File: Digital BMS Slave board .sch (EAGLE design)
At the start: 259 parts, among them J1 S4B-PH-K, J10 S3B-PH-K, J11 S6B-PH-K, J12 MOLEX22-12-406205-7068, J2 S4B-PH-K, J3 S4B-PH-K, J4 S4B-PH-K, J5 S2B-PH-K, J6 S2B-PH-K, J7 S2B-PH-K, J8 S2B-PH-K, J9 S3B-PH-K, Q1 BSS123, Q2 BSS123, Q3 BSS123, Q4 BSS123, Q5 BSS123, Q6 BSS123, SW1 6PIN-DIP-SWITCH, U1 BQ79606A-Q1-HTQFP|48|9VIA, X1 PESD2CAN, X2 PESD2CAN, X3 PESD2CAN, X4 PESD2CAN

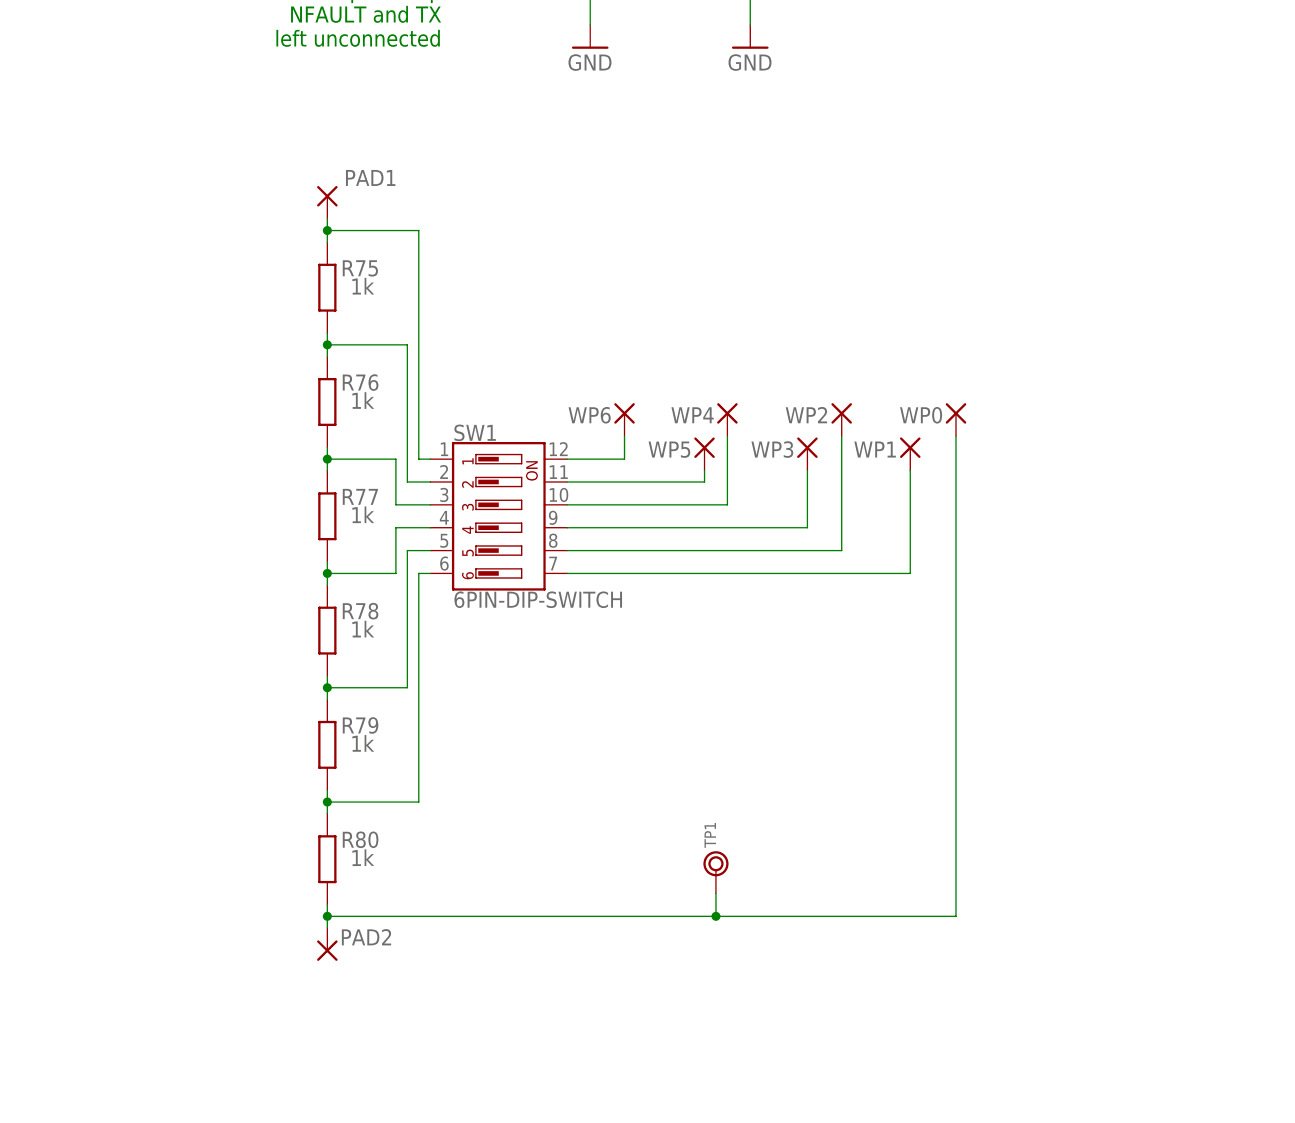
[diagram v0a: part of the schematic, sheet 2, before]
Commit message: Connectors to resistor ladder added
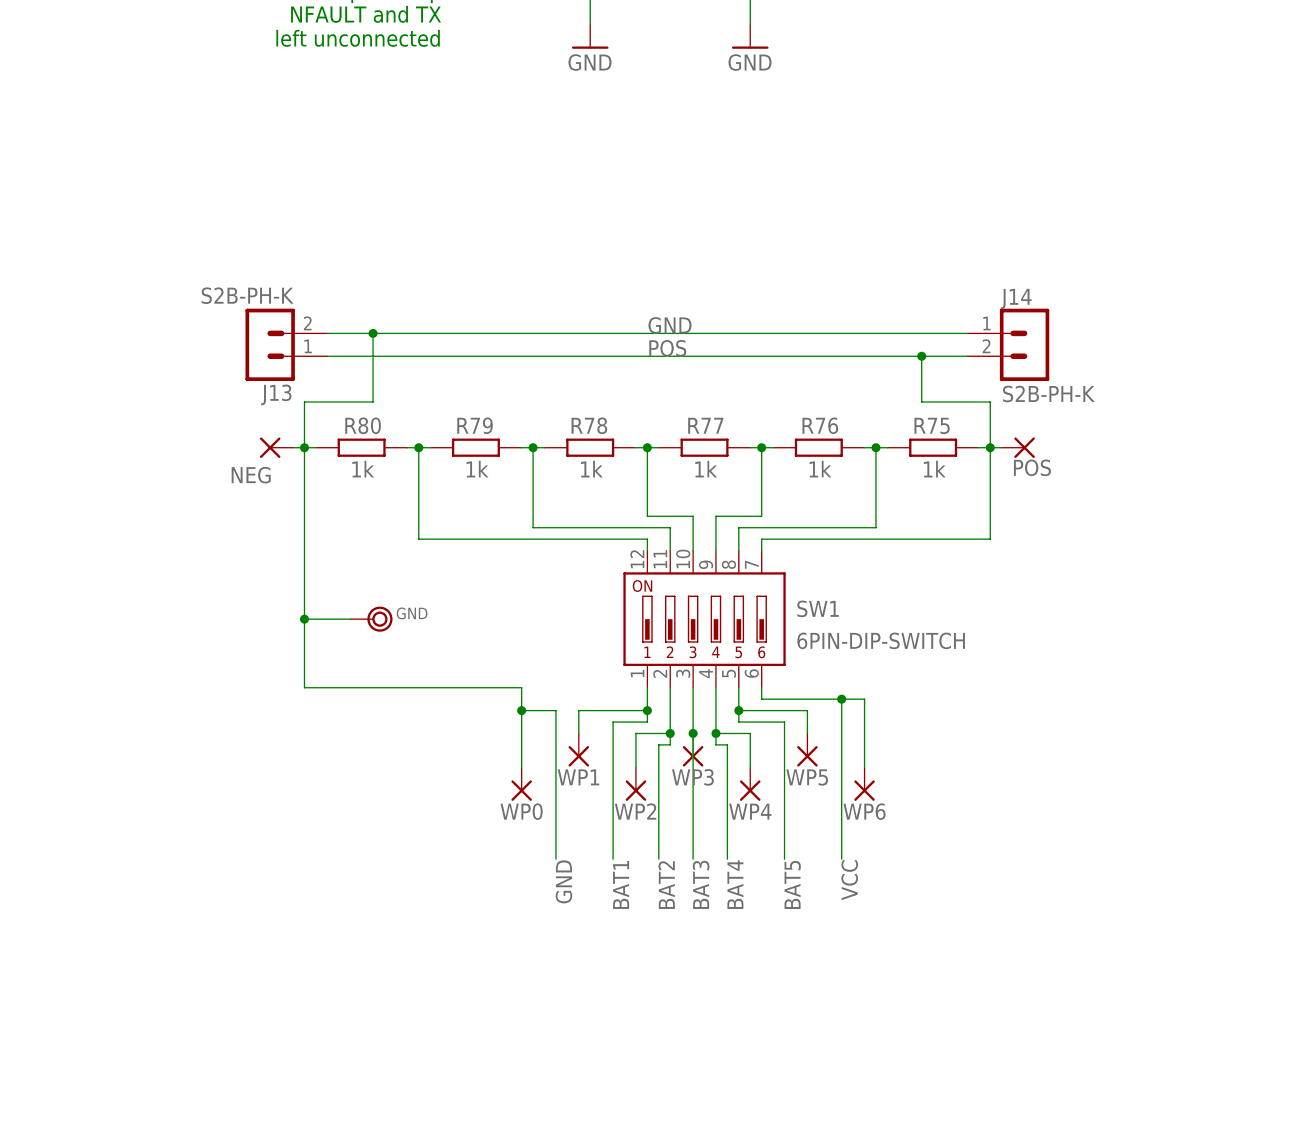
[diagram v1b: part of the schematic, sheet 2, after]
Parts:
- removed PAD1, PAD2: (no value), testing:SMD_PAD
- removed TP1: TEST_RING, testing:TEST_RING
- added GND: TEST_RING, testing:TEST_RING
- added J13, J14: S2B-PH-K, con-jst-ph:S2B-PH-K
- added NEG, POS: (no value), testing:SMD_PAD
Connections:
- removed net N$10: PAD1.P, R75.1, SW1.1
- removed net N$11: PAD2.P, R80.2, TP1.P$1, WP0.P
- removed net N$15: SW1.9, WP3.P
- removed net N$16: SW1.8, WP2.P
- removed net N$17: SW1.7, WP1.P
- removed net N$4: SW1.12, WP6.P
- removed net N$5: SW1.11, WP5.P
- removed net N$7: SW1.10, WP4.P
- new net POS: J13.1, J14.2, POS.P, R75.1, SW1.7
- net BAT1: now also SW1.1, WP1.P
- net BAT2: now also SW1.2, WP2.P
- net BAT3: now also SW1.3, WP3.P
- net BAT4: now also SW1.4, WP4.P
- net BAT5: now also SW1.5, WP5.P
- net GND: now also GND.P$1, J13.2, J14.1, NEG.P, R80.2, WP0.P
- net N$13: now also SW1.12; no longer SW1.6
- net N$14: now also SW1.11; no longer SW1.5
- net N$6: now also SW1.10; no longer SW1.4
- net N$8: now also SW1.9; no longer SW1.3
- net N$9: now also SW1.8; no longer SW1.2
- net VCC: now also SW1.6, WP6.P
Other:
- moved on the sheet: R75, R76, R77, R78, R79, R80, SW1, WP0, WP1, WP2, WP3, WP4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

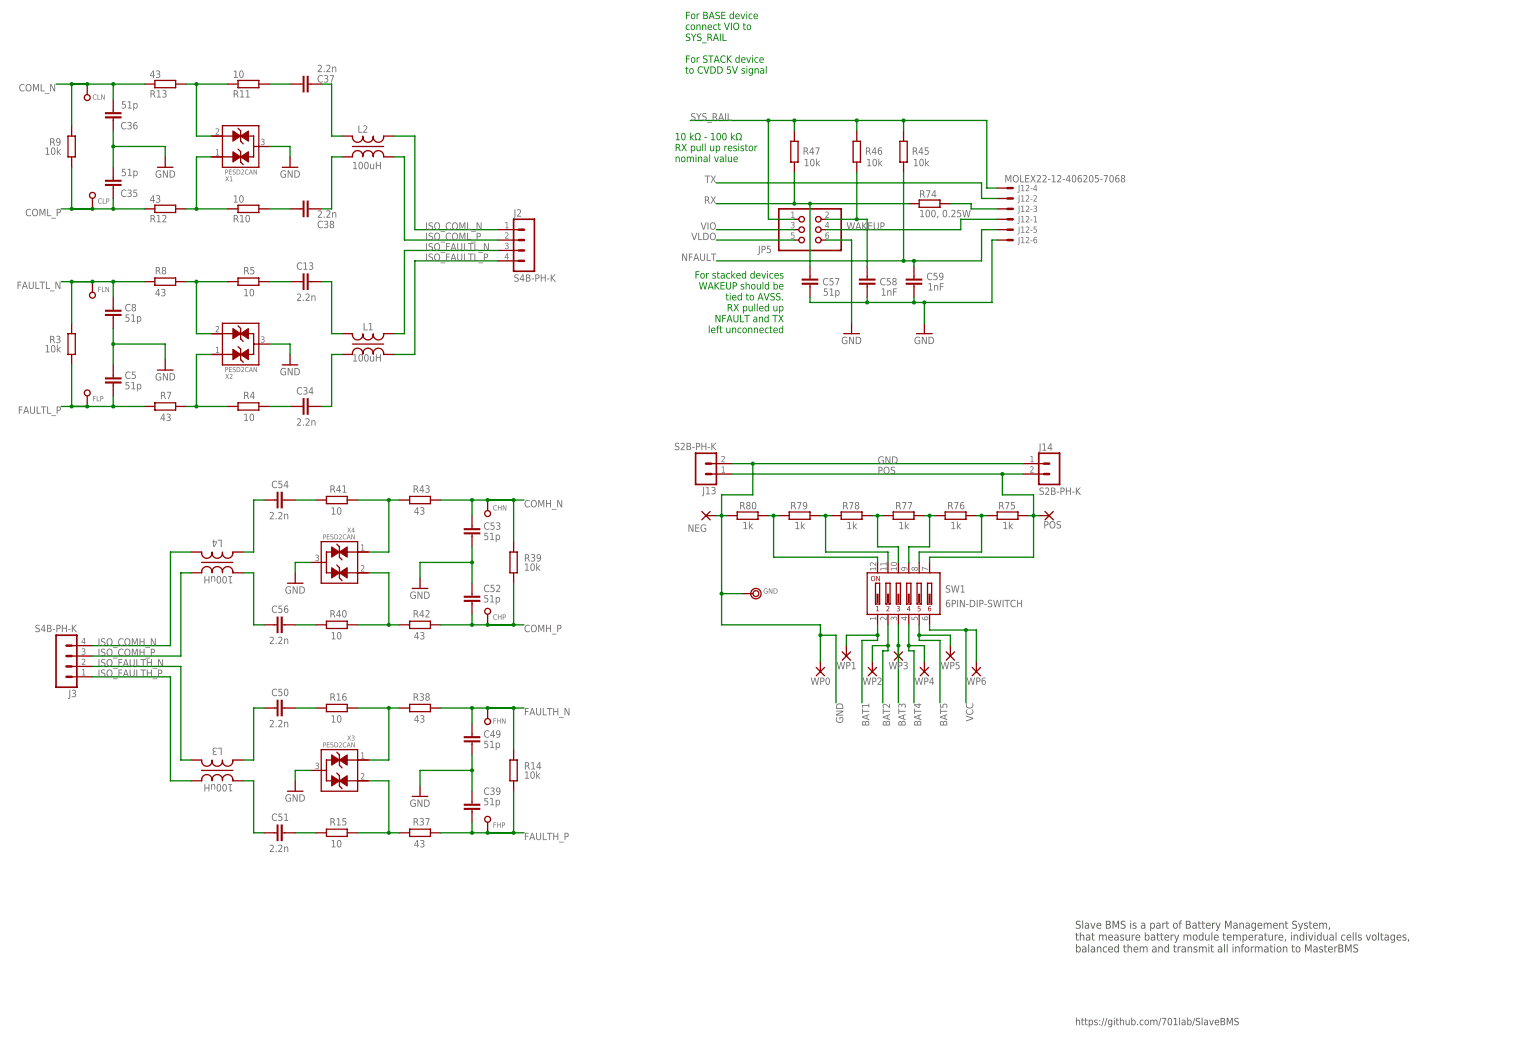
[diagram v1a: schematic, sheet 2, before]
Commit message: Isolation IC added. Power trace fixed
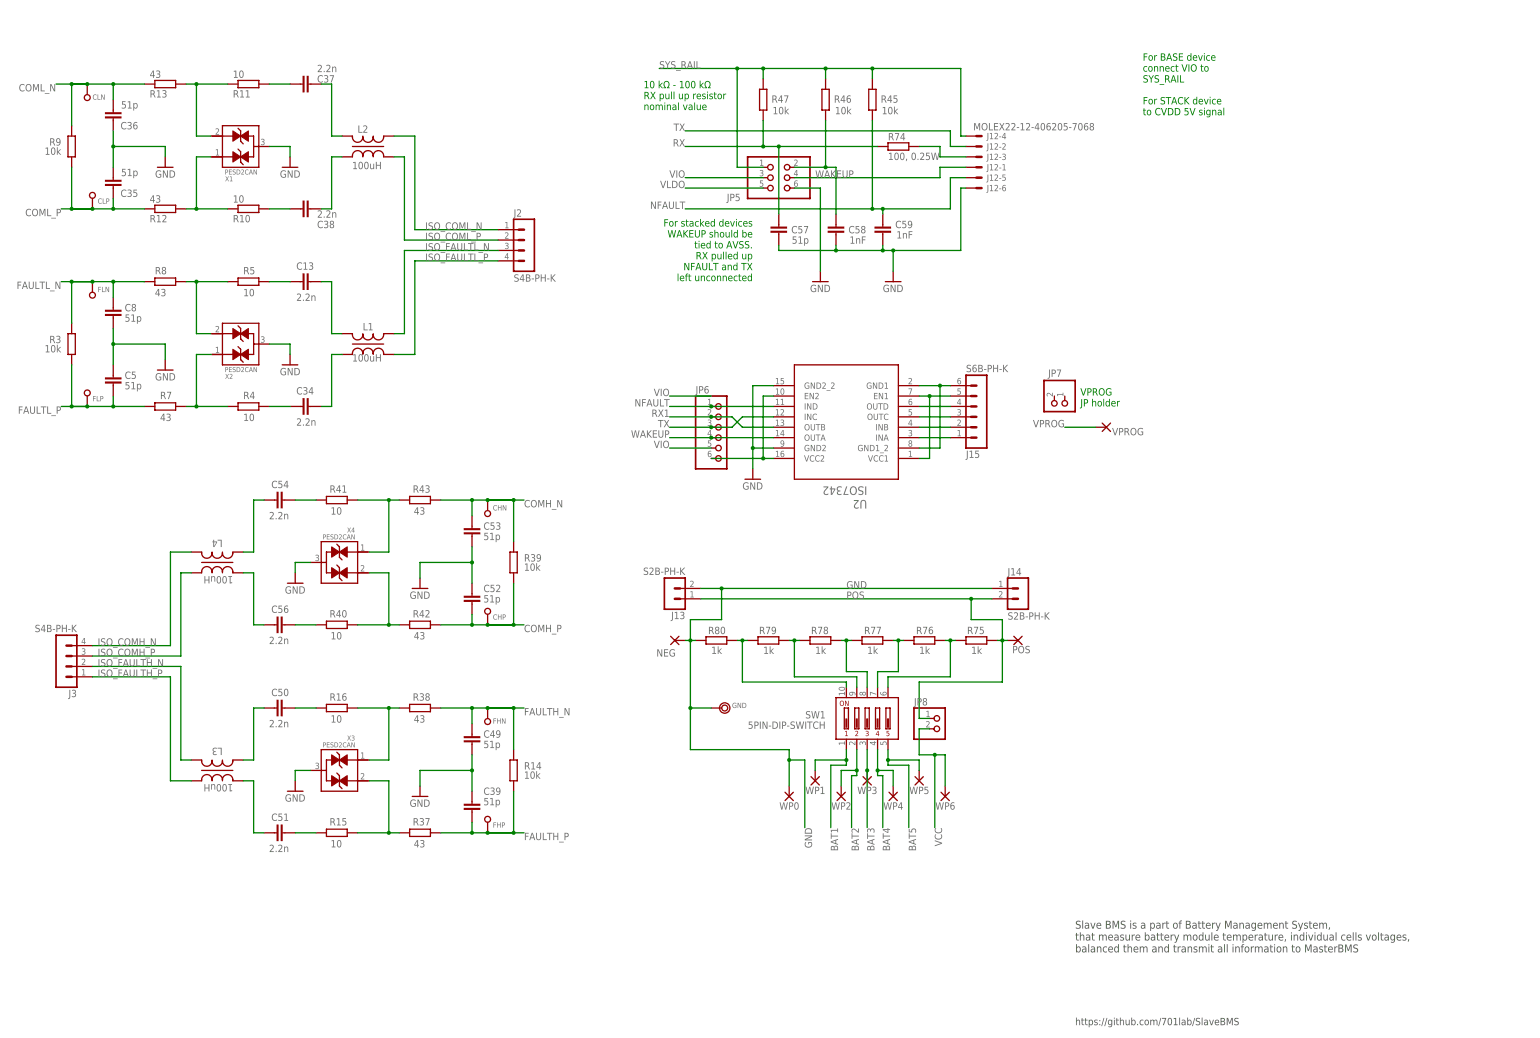
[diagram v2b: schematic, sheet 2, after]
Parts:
- added J15: S6B-PH-K, con-jst-ph:S6B-PH-K
- added JP6: (no value), commonly used connectors:PINHD-1X6-OCT
- added JP7, JP8: (no value), commonly used connectors:PINHD-1X2
- added U2: ISO7342, texas Instrumets:ISO7342
- added VPROG: (no value), testing:SMD_PAD
- SW1: value 6PIN-DIP-SWITCH -> 5PIN-DIP-SWITCH; device buttons and switches:6PIN-DIP-SWITCH -> buttons and switches:5PIN-DIP-SWITCH
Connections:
- removed net N$2: J12-3.S, R74.1
- new net GND2: J15.5, U2.EN1, U2.VCC1
- new net HOST_RX: J15.3, U2.OUTC
- new net HOST_TX: J15.2, U2.INB
- new net N$5: JP6.6, U2.EN2, U2.VCC2
- new net NFL_ISO: J15.4, U2.OUTD
- new net RX1: J12-3.S, JP6.2, R74.1, U2.OUTB
- new net VCC2: J15.6, U2.GND1, U2.GND1_2
- new net WKP_ISO: J15.1, U2.INA
- net GND: now also U2.GND2, U2.GND2_2
- net N$13: now also SW1.10; no longer SW1.12
- net N$14: now also SW1.9; no longer SW1.11
- net N$6: now also SW1.8; no longer SW1.10
- net N$8: now also SW1.7; no longer SW1.9
- net N$9: now also SW1.6; no longer SW1.8
- net NFAULT: now also JP6.1, U2.IND
- net POS: now also JP8.1; no longer SW1.7
- net TX: now also JP6.3, U2.INC
- net VCC: now also JP8.2; no longer SW1.6
- net VIO: now also JP6.5
- net VPROG: now also VPROG.P
- net WAKEUP: now also JP6.4, U2.OUTA
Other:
- note added: "VPROG JP holder"
- moved on the sheet: C12, C57, C58, C59, GND, J12-1, J12-2, J12-3, J12-4, J12-5, J12-6, J13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

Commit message: 123
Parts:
- added JP10, JP9: (no value), pinhead:PINHD-1X1
- C11, C31, C32, C33, C35, C36, C39, C40, C49, C5, C52, C53, C60, C61, C62, C63, C64, C65, C66, C67, C68, C69, C7, C70, C8, C9: device resistor:C-EUC0603 -> Capacitors:C-EU0603
- R10, R100, R11, R12, R13, R14, R15, R16, R17, R18, R19, R2, R22, R23, R24, R25, R26, R27, R28, R29, R3, R37, R38, R39, R4, R40, R41, R42, R43, R45, R46, R47, R48, R49, R5, R51, R52, R53, R54, R55, R56, R57, R58, R59, R60, R62, R65, R7, R74, R8, R9: device resistor:R-EU_R0603 -> Resistors:R-EU0603
- R30, R31, R32, R33, R34, R35, R36: device resistor:R-EU_R1210 -> Resistors:R-EU1210
- RB1, RB2, RB3, RB4, RB5, RB6: device resistor:R-EU_R2512 -> Resistors:R-EU2512
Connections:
- net N$5 renamed VCISO
- net GND: now also JP6.5
- net GND2: now also J15.2; no longer J15.5
- net HOST_RX: now also J15.4; no longer J15.3
- net HOST_TX: now also J15.5; no longer J15.2
- net NFL_ISO: now also J15.3; no longer J15.4
- net VCC2: now also J15.1; no longer J15.6
- net VIO: now also JP9.1; no longer JP6.5
- net WKP_ISO: now also J15.6; no longer J15.1
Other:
- moved on the sheet: J13, J14, J15

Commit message: assembly drawing
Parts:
- C10, C12, C14, C15, C16, C18, C19, C26, C27, C28, C3, C4, C41, C42, C43, C46, C47, C48, C55, C57, C58, C59, C6, C71, C74: device resistor:C-EUC0603 -> Capacitors:C-EU0603
- JP1, JP4: device pinhead:PINHD-2X7 -> commonly used connectors:PINHD-2X7
- JP10, JP9: device pinhead:PINHD-1X1 -> commonly used connectors:PINHD-1X2
- JP5: device pinhead:PINHD-2X3 -> commonly used connectors:PINHD-2X3
- JP6: device commonly used connectors:PINHD-1X6-OCT -> commonly used connectors:PINHD-1X4
- Q1, Q2, Q3, Q4, Q5, Q6: device transistor-small-signal:BSS123 -> Semiconductor_devices:BSS123
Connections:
- new net NC: JP10.1
- net GND: now also JP6.4; no longer JP6.5
- net GND2: now also J15.1, U2.GND1, U2.GND1_2; no longer J15.2, U2.EN1, U2.VCC1
- net NFAULT: now also JP10.2; no longer JP6.1
- net RX1: now also JP6.1; no longer JP6.2
- net TX: now also JP6.2; no longer JP6.3
- net VCC2: now also J15.2, U2.EN1, U2.VCC1; no longer J15.1, U2.GND1, U2.GND1_2
- net VCISO: now also JP9.1; no longer JP6.6
- net VIO: now also JP9.2; no longer JP9.1
- net WAKEUP: now also JP6.3; no longer JP6.4

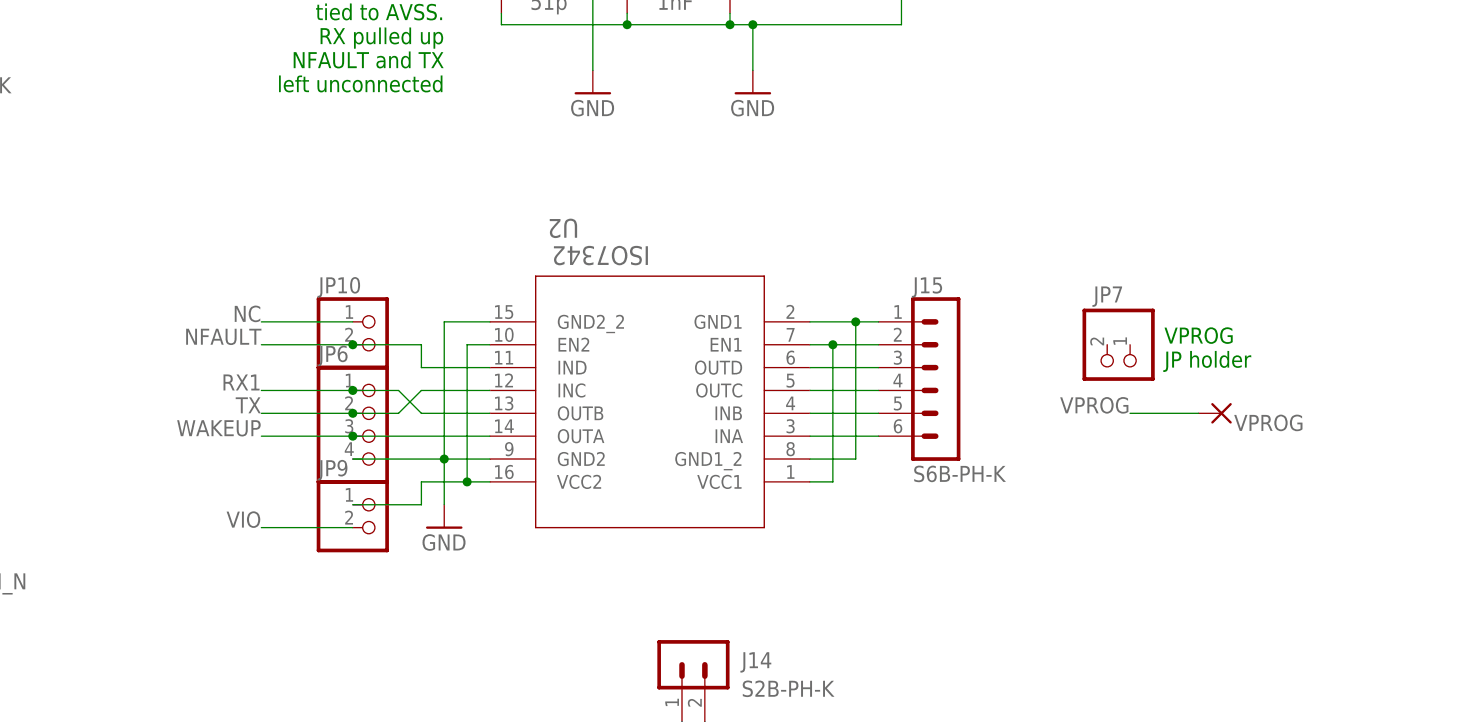
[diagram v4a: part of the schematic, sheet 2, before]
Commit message: pull up at isolation side
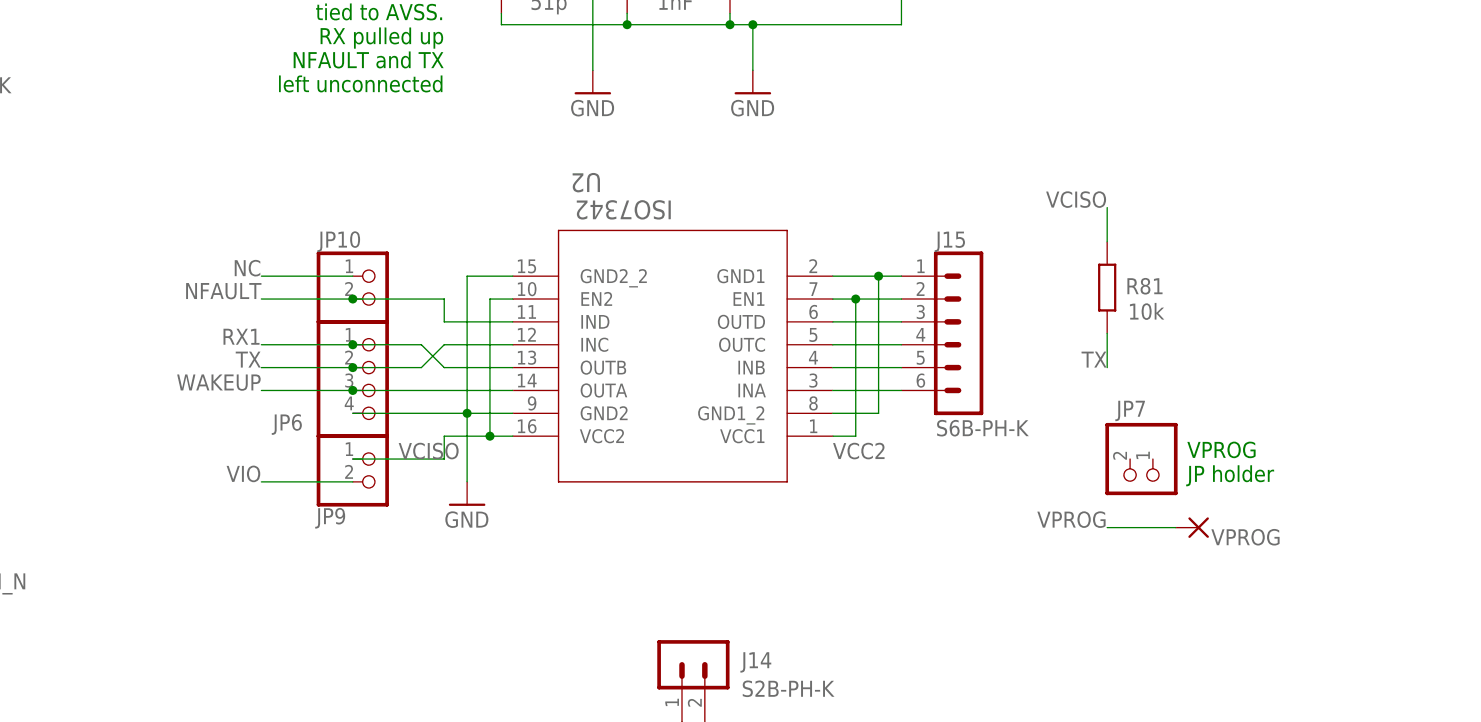
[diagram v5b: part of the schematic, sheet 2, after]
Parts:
- added R81: 10k, Resistors:R-EU0603
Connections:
- net TX: now also R81.1
- net VCISO: now also R81.2
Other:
- moved on the sheet: J15, JP10, JP6, JP7, JP9, U2, VPROG
